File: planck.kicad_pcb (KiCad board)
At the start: 2 copper layers, 113 x 75 mm, 54 parts, among them J1 C128990, J2 USB_C_U262-161N-4BVC11, J3 C128990, SW1 SW_Cherry_MX_1.00u, SW10 SW_Cherry_MX_1.00u, SW11 SW_Cherry_MX_1.00u, SW12 SW_Cherry_MX_1.00u, SW13 SW_Cherry_MX_1.00u, SW14 SW_Cherry_MX_1.00u, SW15 SW_Cherry_MX_1.00u, SW16 SW_Cherry_MX_1.00u, SW17 SW_Cherry_MX_1.00u, SW18 SW_Cherry_MX_1.00u, SW19 SW_Cherry_MX_1.00u, SW2 SW_Cherry_MX_1.00u, SW20 SW_Cherry_MX_1.00u, SW21 SW_Cherry_MX_1.00u, SW22 SW_Cherry_MX_1.00u, SW23 SW_Cherry_MX_1.00u, SW24 SW_Cherry_MX_1.00u, SW3 SW_Cherry_MX_1.00u, SW4 SW_Cherry_MX_1.00u, SW5 SW_Cherry_MX_1.00u, SW6 SW_Cherry_MX_1.00u, SW7 SW_Cherry_MX_1.00u, SW8 SW_Cherry_MX_1.00u, SW9 SW_Cherry_MX_1.00u, U2 RP2040

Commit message: some modifications
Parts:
- removed J3: C128990, C128990:C128990_3.5MM_TRRS
- removed U2: RP2040, RP2040_minimal:RP2040-QFN-56
- added U1: RP2040, RP2040_minimal:RP2040-QFN-56, B.Cu at (139.0, 97.5)
- added Y1: 32M, Crystal:Crystal_SMD_3225-4Pin_3.2x2.5mm, B.Cu at (133.9, 121.2)
- J1: value C128990 -> USB_C_U262-161N-4BVC11; footprint C128990:C128990_3.5MM_TRRS -> josh-connectors:USB_C_U262-161N-4BVC11
- moved J2 37.8 mm to (101.2, 65.2)
- moved J1 4.66 mm to (177.0, 64.6)
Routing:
- net r1: track 239.1 -> 118.0 mm, vias 4 -> 3
- net Net-(J2-PadA5): track 2.96 -> 0.00 mm
- net Net-(J2-PadB5): track 2.53 -> 0.00 mm
- net r3: track 104.2 -> 103.2 mm

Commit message: MX version complete
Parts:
- added C1: 2.2uF ±10% 10V, Resistor_SMD:R_0201_0603Metric, B.Cu at (99.1, 69.7)
- added C10: 100nF ±10% 25V 0201, Resistor_SMD:R_0201_0603Metric, B.Cu at (138.2, 92.5)
- added C11: 100nF ±10% 25V 0201, Resistor_SMD:R_0201_0603Metric, B.Cu at (144.0, 98.5)
- added C12: 100nF ±10% 25V 0201, Resistor_SMD:R_0201_0603Metric, B.Cu at (138.3, 102.5)
- added C13: 100nF ±10% 25V 0201, Resistor_SMD:R_0201_0603Metric, B.Cu at (138.9, 92.5)
- added C14: 1uF ±20% 6.3V 0201, Capacitor_SMD:C_0201_0603Metric, B.Cu at (137.0, 92.5)
- added C15: 100nF ±10% 25V 0201, Resistor_SMD:R_0201_0603Metric, B.Cu at (136.2, 92.5)
- added C16: 100nF ±10% 25V 0201, Resistor_SMD:R_0201_0603Metric, B.Cu at (137.2, 102.5)
- added C2: 2.2uF ±10% 10V, Resistor_SMD:R_0201_0603Metric, B.Cu at (99.0, 74.7)
- added C3: 22pF ±5% 50V 0603, Resistor_SMD:R_0201_0603Metric, B.Cu at (141.5, 104.4)
- added C4: 22pF ±5% 50V 0603, Resistor_SMD:R_0201_0603Metric, B.Cu at (136.5, 104.9)
- added C5: 100nF ±10% 25V 0201, Resistor_SMD:R_0201_0603Metric, B.Cu at (144.0, 92.6)
- added C6: 1uF ±20% 6.3V 0201, Capacitor_SMD:C_0201_0603Metric, B.Cu at (134.1, 94.2)
- added C7: 100nF ±10% 25V 0201, Resistor_SMD:R_0201_0603Metric, B.Cu at (134.1, 94.9)
- added C8: 100nF ±10% 25V 0201, Resistor_SMD:R_0201_0603Metric, B.Cu at (144.0, 94.2)
- added C9: 100nF ±10% 25V 0201, Resistor_SMD:R_0201_0603Metric, B.Cu at (134.1, 98.4)
- added H1: MountingHole, MountingHole:MountingHole_2.7mm_M2.5, F.Cu at (101.0, 78.5)
- added H2: MountingHole, MountingHole:MountingHole_2.7mm_M2.5, F.Cu at (177.0, 78.5)
- added H3: MountingHole, MountingHole:MountingHole_2.7mm_M2.5, F.Cu at (177.0, 116.5)
- added H4: MountingHole, MountingHole:MountingHole_2.7mm_M2.5, F.Cu at (101.0, 116.4)
- added R3: 1kΩ ±1% 50mW 0201, Resistor_SMD:R_0201_0603Metric, B.Cu at (137.6, 103.9)
- added R4: 100Ω ±1% 50mW, Resistor_SMD:R_0201_0603Metric, B.Cu at (144.0, 95.0)
- added R5: 27Ω ±1% 50mW 0201, Resistor_SMD:R_0201_0603Metric, B.Cu at (137.9, 91.1)
- added R6: 27Ω ±1% 50mW 0201, Resistor_SMD:R_0201_0603Metric, B.Cu at (137.2, 91.1)
- added R7: 100Ω ±1% 50mW, Resistor_SMD:R_0201_0603Metric, B.Cu at (144.0, 95.7)
- added R8: 10kΩ ±1% 50mW 0201, Resistor_SMD:R_0201_0603Metric, B.Cu at (144.0, 93.4)
- added R9: 1kΩ ±1% 50mW 0201, Resistor_SMD:R_0201_0603Metric, B.Cu at (142.1, 92.6)
- added SW25: SW_Push, Switches:TSC005A1618A03, B.Cu at (139.0, 75.0)
- added U2: ME6219C33M5G, Package_TO_SOT_SMD:SOT-23-5, B.Cu at (99.7, 72.2)
- added U3: W25Q16JVUXIQ, Package_SON:SON-8-1EP_3x2mm_P0.5mm_EP1.4x1.6mm, B.Cu at (143.1, 90.9)
- D1, D10, D11, D12, D13, D14, D15, D16, D17, D18, D19, D2, D20, D21, D22, D23, D24, D3, D4, D5, D6, D7, D8, D9: value 1N4148W -> 1N4148W,100V 150mA 4ns T4
- J1, J2: footprint josh-connectors:USB_C_U262-161N-4BVC11 -> josh-connectors:USB_C_TYPE-C-31-M-14
- U1: value RP2040 -> RP2040 ARM Cortex-M0 133MHz; footprint RP2040_minimal:RP2040-QFN-56 -> Package_DFN_QFN:QFN-56-1EP_7x7mm_P0.4mm_EP3.2x3.2mm_ThermalVias
- Y1: value 32M -> 32MHz ±10ppm 20pF SMD3225-4P
- moved R2 38.9 mm to (102.6, 69.0), turned to 180 degrees
- moved R1 37.4 mm to (99.1, 69.0), turned to 0 degrees
- moved Y1 16.5 mm to (139.0, 105.5), turned to -135 degrees
- moved J2 0.85 mm to (101.2, 64.3)
- moved J1 0.22 mm to (177.0, 64.4), turned to 0 degrees
- turned U1 to 180 degrees
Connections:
- net /d+ renamed /D-
- net /d- renamed /D+
- U1 pad 1: unconnected-(U1-Pad1) -> /V3V3
- U1 pad 10: unconnected-(U1-Pad10) -> /V3V3
- U1 pad 14: unconnected-(U1-Pad14) -> c6
- U1 pad 15: unconnected-(U1-Pad15) -> c5
- U1 pad 16: unconnected-(U1-Pad16) -> c4
- U1 pad 19: unconnected-(U1-Pad19) -> GND
- U1 pad 2: unconnected-(U1-Pad2) -> /tx0
- U1 pad 20: unconnected-(U1-Pad20) -> /X32MI
- U1 pad 21: unconnected-(U1-Pad21) -> /X32MO
- U1 pad 22: unconnected-(U1-Pad22) -> /V3V3
- U1 pad 23: unconnected-(U1-Pad23) -> /V1V1
- U1 pad 28: unconnected-(U1-Pad28) -> r4
- U1 pad 29: unconnected-(U1-Pad29) -> r3
- U1 pad 3: unconnected-(U1-Pad3) -> /rx0
- U1 pad 30: unconnected-(U1-Pad30) -> c3
- U1 pad 31: unconnected-(U1-Pad31) -> c2
- U1 pad 32: unconnected-(U1-Pad32) -> c1
- U1 pad 33: unconnected-(U1-Pad33) -> /V3V3
- U1 pad 4: unconnected-(U1-Pad4) -> r1
- U1 pad 42: unconnected-(U1-Pad42) -> /V3V3
- U1 pad 43: unconnected-(U1-Pad43) -> /V3V3
- U1 pad 44: unconnected-(U1-Pad44) -> /V3V3
- U1 pad 45: unconnected-(U1-Pad45) -> /V1V1
- U1 pad 46: unconnected-(U1-Pad46) -> Net-(R6-Pad1)
- U1 pad 47: unconnected-(U1-Pad47) -> Net-(R5-Pad1)
- U1 pad 48: unconnected-(U1-Pad48) -> /V3V3
- U1 pad 49: unconnected-(U1-Pad49) -> /V3V3
- U1 pad 5: unconnected-(U1-Pad5) -> r2
- U1 pad 50: unconnected-(U1-Pad50) -> /V1V1
- U1 pad 51: unconnected-(U1-Pad51) -> /QSPI_SD3
- U1 pad 52: unconnected-(U1-Pad52) -> /QSPI_CLK
- U1 pad 53: unconnected-(U1-Pad53) -> /QSPI_SD0
- U1 pad 54: unconnected-(U1-Pad54) -> /QSPI_SD2
- U1 pad 55: unconnected-(U1-Pad55) -> /QSPI_SD1
- U1 pad 56: unconnected-(U1-Pad56) -> /QSPI_SS
- U1 pad 57: unconnected-(U1-Pad57) -> GND
- Y1 pad 3: /X32MO -> Net-(C4-Pad1)
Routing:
- net /VBUS: track 0.00 -> 123.6 mm, vias 0 -> 4
- net /V3V3: track 0.00 -> 76.6 mm, vias 0 -> 2
- net Net-(J1-PadA6): track 0.00 -> 65.6 mm, vias 0 -> 2
- net Net-(J1-PadA7): track 0.00 -> 64.9 mm, vias 0 -> 2
- net /D-: track 0.00 -> 59.5 mm, vias 0 -> 2
- net /D+: track 0.00 -> 58.6 mm
- net r2: track 182.5 -> 124.3 mm
- net c6: track 62.4 -> 118.3 mm, vias 4 -> 7
- net r1: track 118.0 -> 165.4 mm, vias 3 -> 4
- net c5: track 62.4 -> 102.8 mm, vias 4 -> 7
- net c1: track 62.5 -> 101.4 mm, vias 4 -> 5
- net c4: track 62.4 -> 91.1 mm, vias 4 -> 7
- net Net-(R9-Pad1): track 0.00 -> 23.9 mm, vias 0 -> 2
- net r4: track 104.2 -> 127.3 mm, vias 0 -> 2
- net r3: track 103.2 -> 119.4 mm, vias 0 -> 2
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- added copper zone on B.Cu, net /V3V3
- added copper zone on F.Cu, net GND
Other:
- outline, holes or cut-outs redrawn
- board text added: "boot"

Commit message: add libraries
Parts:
- U1: footprint Package_DFN_QFN:QFN-56-1EP_7x7mm_P0.4mm_EP3.2x3.2mm_ThermalVias -> MCU_RaspberryPi_and_Boards:RP2040-QFN-56

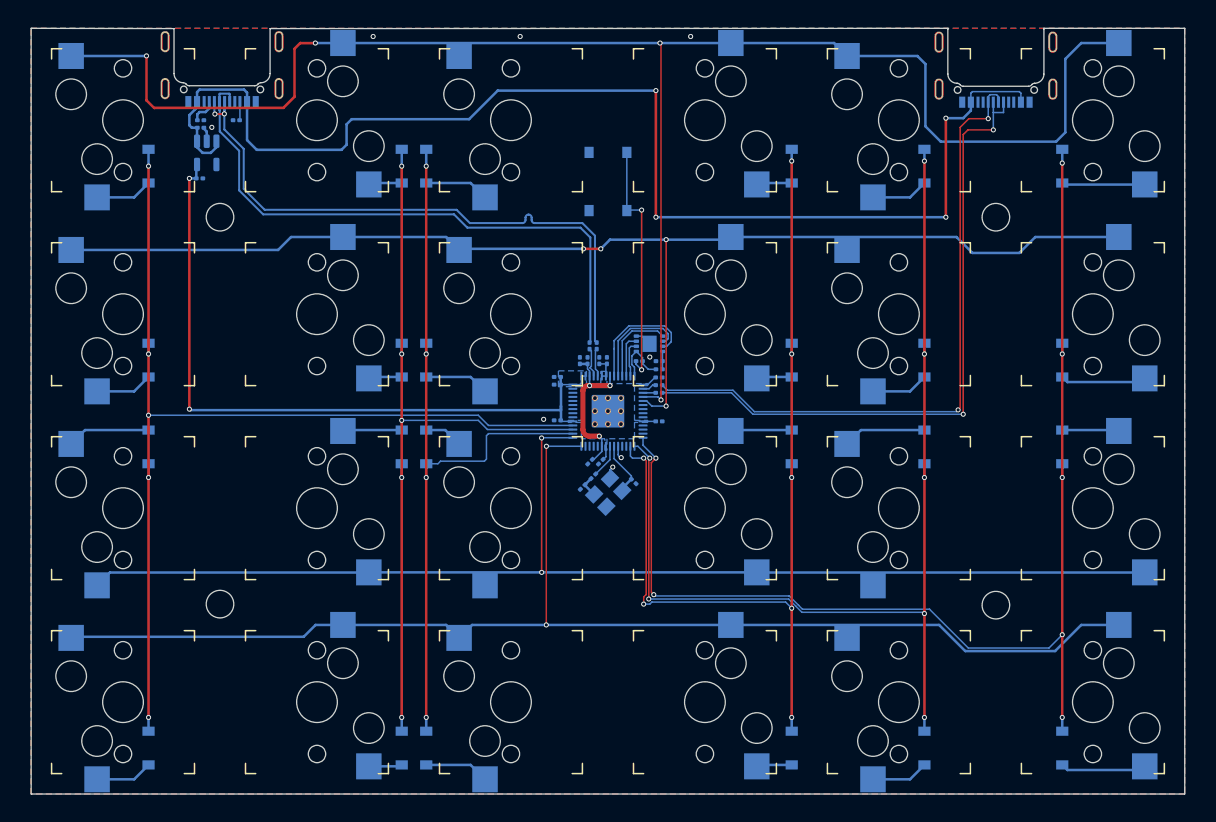
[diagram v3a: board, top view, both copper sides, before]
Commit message: add choc libraries
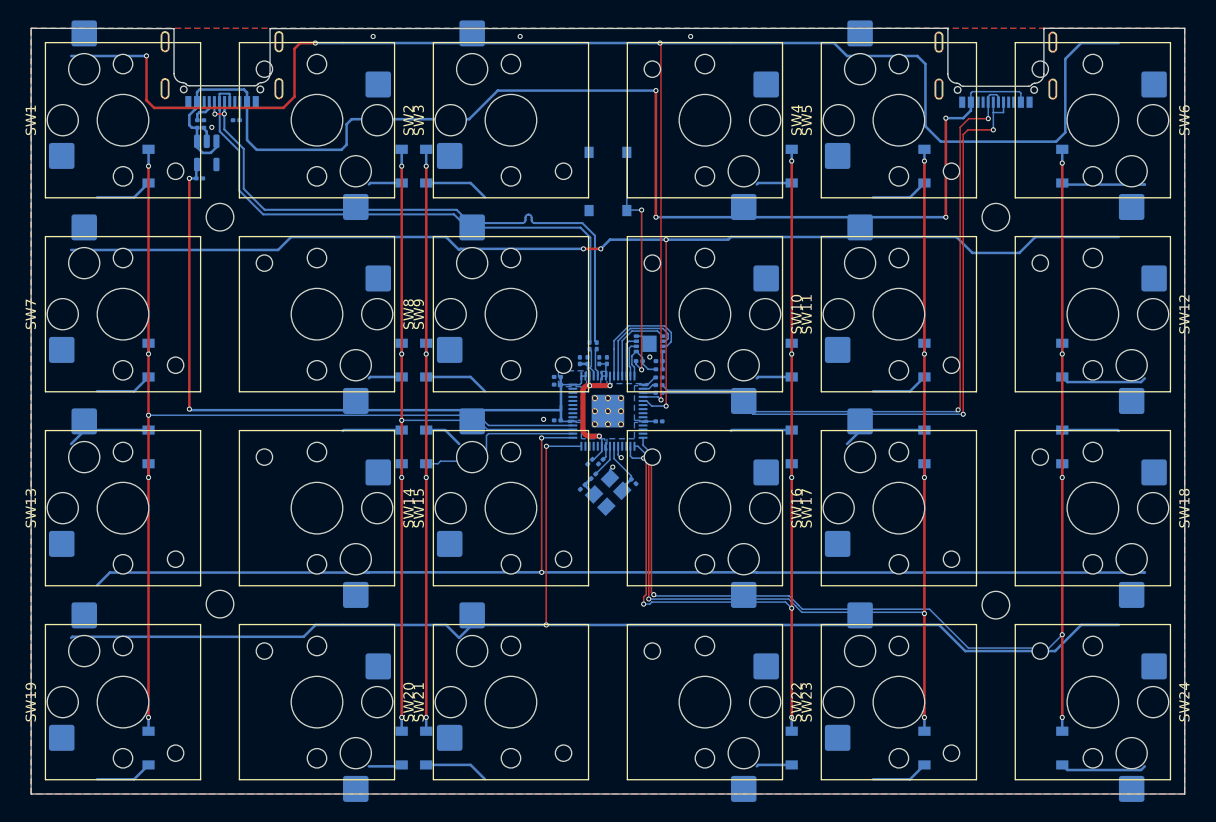
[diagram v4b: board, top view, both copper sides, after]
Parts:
- SW1, SW10, SW11, SW12, SW13, SW14, SW15, SW16, SW17, SW18, SW19, SW2, SW20, SW21, SW22, SW23, SW24, SW3, SW4, SW5, SW6, SW7, SW8, SW9: footprint Switches:SW_Cherry_MX_1.00u_Plate_HS -> Switch_Keyboard_Hotswap_Kailh:SW_Hotswap_Kailh_Choc_V1V2
- turned SW1 to 90 degrees
- turned SW10 to -90 degrees
- turned SW11 to 90 degrees
- turned SW12 to -90 degrees
- turned SW13 to 90 degrees
- turned SW14 to -90 degrees
- turned SW15 to 90 degrees
- turned SW16 to -90 degrees
- turned SW17 to 90 degrees
- turned SW18 to -90 degrees
- turned SW19 to 90 degrees
- turned SW2 to -90 degrees
- turned SW20 to -90 degrees
- turned SW21 to 90 degrees
- turned SW22 to -90 degrees
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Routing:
- net /VBUS: track 123.6 -> 684.4 mm, vias 4 -> 31
- net c6: track 118.3 -> 0.00 mm, vias 7 -> 0
- net c5: track 102.8 -> 0.00 mm, vias 7 -> 0
- net c4: track 91.1 -> 0.00 mm, vias 7 -> 0
- net Net-(J1-PadA6): track 65.6 -> 0.00 mm, vias 2 -> 0
- net Net-(J1-PadA7): track 64.9 -> 0.00 mm, vias 2 -> 0
- net /D-: track 59.5 -> 0.00 mm, vias 2 -> 0
- net /D+: track 58.6 -> 0.00 mm
- net GND: vias 8 -> 7
- net /QSPI_SS: vias 0 -> 1

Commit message: main layouts
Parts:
- removed J1: USB_C_U262-161N-4BVC11, josh-connectors:USB_C_TYPE-C-31-M-14
- removed R4, R7: 100Ω ±1% 50mW, Resistor_SMD:R_0201_0603Metric
- added C17: 100nF ±10% 25V 0201, Resistor_SMD:R_0201_0603Metric, B.Cu at (143.8, 131.4)
- added C18: 100nF ±10% 25V 0201, Resistor_SMD:R_0201_0603Metric, B.Cu at (152.3, 101.5)
- added C19: 100nF ±10% 25V 0201, Resistor_SMD:R_0201_0603Metric, B.Cu at (191.2, 101.4)
- added C20: 100nF ±10% 25V 0201, Resistor_SMD:R_0201_0603Metric, B.Cu at (115.2, 63.5)
- added C21: 100nF ±10% 25V 0201, Resistor_SMD:R_0201_0603Metric, B.Cu at (96.2, 63.4)
- added C22: 100nF ±10% 25V 0201, Resistor_SMD:R_0201_0603Metric, B.Cu at (162.8, 93.5)
- added C23: 100nF ±10% 25V 0201, Resistor_SMD:R_0201_0603Metric, B.Cu at (86.8, 93.6)
- added C24: 100nF ±10% 25V 0201, Resistor_SMD:R_0201_0603Metric, B.Cu at (124.8, 131.6)
- added C25: 100nF ±10% 25V 0201, Resistor_SMD:R_0201_0603Metric, B.Cu at (115.2, 101.5)
- added C26: 100nF ±10% 25V 0201, Resistor_SMD:R_0201_0603Metric, B.Cu at (172.2, 101.5)
- added C27: 100nF ±10% 25V 0201, Resistor_SMD:R_0201_0603Metric, B.Cu at (181.8, 93.6)
- added C28: 100nF ±10% 25V 0201, Resistor_SMD:R_0201_0603Metric, B.Cu at (125.7, 93.5)
- added C29: 100nF ±10% 25V 0201, Resistor_SMD:R_0201_0603Metric, B.Cu at (146.3, 94.9)
- added C30: 100nF ±10% 25V 0201, Resistor_SMD:R_0201_0603Metric, B.Cu at (105.8, 93.5)
- added C31: 100nF ±10% 25V 0201, Resistor_SMD:R_0201_0603Metric, B.Cu at (105.8, 131.4)
- added C32: 100nF ±10% 25V 0201, Resistor_SMD:R_0201_0603Metric, B.Cu at (96.2, 101.5)
- added C33: 100nF ±10% 25V 0201, Resistor_SMD:R_0201_0603Metric, B.Cu at (133.4, 101.5)
- added C34: 100nF ±10% 25V 0201, Resistor_SMD:R_0201_0603Metric, B.Cu at (191.2, 63.4)
- added C35: 100nF ±10% 25V 0201, Resistor_SMD:R_0201_0603Metric, B.Cu at (172.2, 63.4)
- added C36: 100nF ±10% 25V 0201, Resistor_SMD:R_0201_0603Metric, B.Cu at (152.3, 63.5)
- added C37: 100nF ±10% 25V 0201, Resistor_SMD:R_0201_0603Metric, B.Cu at (131.2, 62.2)
- added C38: 100nF ±10% 25V 0201, Resistor_SMD:R_0201_0603Metric, B.Cu at (86.8, 131.4)
- added C39: 100nF ±10% 25V 0201, Resistor_SMD:R_0201_0603Metric, B.Cu at (181.8, 131.4)
- added C40: 100nF ±10% 25V 0201, Resistor_SMD:R_0201_0603Metric, B.Cu at (162.8, 131.4)
- added D25: WS2812B, MCU_RaspberryPi_and_Boards:WS2812_6028_REV, F.Cu at (91.5, 64.2)
- added D26: WS2812B, MCU_RaspberryPi_and_Boards:WS2812_6028_REV, F.Cu at (110.5, 64.3)
- added D27: WS2812B, MCU_RaspberryPi_and_Boards:WS2812_6028_REV_S, F.Cu at (129.5, 64.3)
- added D28: WS2812B, MCU_RaspberryPi_and_Boards:WS2812_6028_REV_S, F.Cu at (148.5, 64.3)
- added D29: WS2812B, MCU_RaspberryPi_and_Boards:WS2812_6028_REV, F.Cu at (167.5, 64.2)
- added D30: WS2812B, MCU_RaspberryPi_and_Boards:WS2812_6028_REV, F.Cu at (186.5, 64.2)
- added D31: WS2812B, MCU_RaspberryPi_and_Boards:WS2812_6028_REV, F.Cu at (186.5, 92.8)
- added D32: WS2812B, MCU_RaspberryPi_and_Boards:WS2812_6028_REV, F.Cu at (167.5, 92.7)
- added D33: WS2812B, MCU_RaspberryPi_and_Boards:WS2812_6028_REV_S, F.Cu at (148.5, 92.7)
- added D34: WS2812B, MCU_RaspberryPi_and_Boards:WS2812_6028_REV_S, F.Cu at (129.5, 92.7)
- added D35: WS2812B, MCU_RaspberryPi_and_Boards:WS2812_6028_REV, F.Cu at (110.5, 92.7)
- added D36: WS2812B, MCU_RaspberryPi_and_Boards:WS2812_6028_REV, F.Cu at (91.5, 92.8)
- added D37: WS2812B, MCU_RaspberryPi_and_Boards:WS2812_6028_REV, F.Cu at (91.5, 102.3)
- added D38: WS2812B, MCU_RaspberryPi_and_Boards:WS2812_6028_REV, F.Cu at (110.5, 102.3)
- added D39: WS2812B, MCU_RaspberryPi_and_Boards:WS2812_6028_REV_S, F.Cu at (129.5, 102.3)
- added D40: WS2812B, MCU_RaspberryPi_and_Boards:WS2812_6028_REV_S, F.Cu at (148.5, 102.3)
- added D41: WS2812B, MCU_RaspberryPi_and_Boards:WS2812_6028_REV, F.Cu at (167.5, 102.3)
- added D42: WS2812B, MCU_RaspberryPi_and_Boards:WS2812_6028_REV, F.Cu at (186.5, 102.2)
- added D43: WS2812B, MCU_RaspberryPi_and_Boards:WS2812_6028_REV, F.Cu at (186.5, 130.7)
- added D44: WS2812B, MCU_RaspberryPi_and_Boards:WS2812_6028_REV, F.Cu at (167.5, 130.7)
- added D45: WS2812B, MCU_RaspberryPi_and_Boards:WS2812_6028_REV, F.Cu at (148.5, 130.7)
- added D46: WS2812B, MCU_RaspberryPi_and_Boards:WS2812_6028_REV, F.Cu at (129.5, 130.8)
- added D47: WS2812B, MCU_RaspberryPi_and_Boards:WS2812_6028_REV, F.Cu at (110.5, 130.7)
- added D48: WS2812B, MCU_RaspberryPi_and_Boards:WS2812_6028_REV, F.Cu at (91.5, 130.7)
- SW1, SW10, SW11, SW12, SW13, SW14, SW15, SW16, SW17, SW18, SW19, SW2, SW20, SW21, SW22, SW23, SW24, SW3, SW4, SW5, SW6, SW7, SW8, SW9: value SW_Cherry_MX_1.00u -> SW_Hotswap_Kailh_Choc_V1_1u; footprint Switch_Keyboard_Hotswap_Kailh:SW_Hotswap_Kailh_Choc_V1V2 -> Switch_Keyboard_Kailh:SW_Hotswap_Kailh_Choc_V1
- moved C1 46.9 mm to (145.3, 77.8), turned to -90 degrees
- moved U2 43.6 mm to (142.8, 78.5), turned to 180 degrees
- moved C2 41.4 mm to (140.3, 77.8), turned to -90 degrees
- moved R1 38.7 mm to (137.8, 68.9), turned to -90 degrees
- moved R2 38.2 mm to (140.8, 68.9), turned to -90 degrees
- moved J2 37.8 mm to (139.0, 64.3)
- moved SW25 29.4 mm to (158.0, 97.5), turned to 0 degrees
- moved D15 19.8 mm to (134.9, 115.3), turned to 0 degrees
- moved D9 18.8 mm to (134.9, 79.7), turned to 0 degrees
- moved D21 18.8 mm to (134.9, 117.7), turned to 0 degrees
- moved D18 16.6 mm to (191.9, 115.3), turned to 0 degrees
- moved D13 16.4 mm to (86.1, 115.3), turned to 180 degrees
- moved D17 16.4 mm to (162.1, 115.3), turned to 180 degrees
- moved D12 15.4 mm to (191.9, 79.7), turned to 0 degrees
- moved D24 15.4 mm to (191.9, 117.7), turned to 0 degrees
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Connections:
- D10 pad 1: Net-(D10-Pad1) -> Net-(D10-K)
- D12 pad 1: Net-(D12-Pad1) -> Net-(D12-K)
- D13 pad 1: Net-(D13-Pad1) -> Net-(D13-K)
- D15 pad 1: Net-(D15-Pad1) -> Net-(D15-K)
- D17 pad 1: Net-(D17-Pad1) -> Net-(D17-K)
- D19 pad 1: Net-(D19-Pad1) -> Net-(D19-K)
- D2 pad 1: Net-(D2-Pad1) -> Net-(D2-K)
- D21 pad 1: Net-(D21-Pad1) -> Net-(D21-K)
- D23 pad 1: Net-(D23-Pad1) -> Net-(D23-K)
- D4 pad 1: Net-(D4-Pad1) -> Net-(D4-K)
- D6 pad 1: Net-(D6-Pad1) -> Net-(D6-K)
- D8 pad 1: Net-(D8-Pad1) -> Net-(D8-K)
- SW10 pad 1: r2 -> Net-(D10-K)
- SW10 pad 2: Net-(D10-Pad1) -> r2
- SW12 pad 1: r2 -> Net-(D12-K)
- SW12 pad 2: Net-(D12-Pad1) -> r2
- SW13 pad 1: r3 -> Net-(D13-K)
- SW13 pad 2: Net-(D13-Pad1) -> r3
- SW15 pad 1: r3 -> Net-(D15-K)
- SW15 pad 2: Net-(D15-Pad1) -> r3
- SW17 pad 1: r3 -> Net-(D17-K)
- SW17 pad 2: Net-(D17-Pad1) -> r3
- SW19 pad 1: Net-(D19-Pad1) -> r4
- SW19 pad 2: r4 -> Net-(D19-K)
- SW2 pad 1: r1 -> Net-(D2-K)
- SW2 pad 2: Net-(D2-Pad1) -> r1
- SW21 pad 1: Net-(D21-Pad1) -> r4
- SW21 pad 2: r4 -> Net-(D21-K)
- SW23 pad 1: Net-(D23-Pad1) -> r4
- SW23 pad 2: r4 -> Net-(D23-K)
- SW4 pad 1: r1 -> Net-(D4-K)
- SW4 pad 2: Net-(D4-Pad1) -> r1
- SW6 pad 1: r1 -> Net-(D6-K)
- SW6 pad 2: Net-(D6-Pad1) -> r1
- SW8 pad 1: r2 -> Net-(D8-K)
- SW8 pad 2: Net-(D8-Pad1) -> r2
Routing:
- net /VBUS: track 684.4 -> 356.5 mm, vias 31 -> 0
- net c3: track 76.3 -> 4.60 mm, vias 4 -> 0
- net /V3V3: track 76.6 -> 10.2 mm, vias 2 -> 0
- net c1: track 101.4 -> 42.2 mm, vias 5 -> 2
- net r1: track 165.4 -> 108.0 mm, vias 4 -> 2
- net c5: track 0.00 -> 42.3 mm, vias 0 -> 2
- net Net-(D30-DOUT): track 0.00 -> 40.5 mm, vias 0 -> 2
- net Net-(D42-DOUT): track 0.00 -> 40.3 mm, vias 0 -> 2
- net c6: track 0.00 -> 40.3 mm, vias 0 -> 2
- net c4: track 0.00 -> 40.3 mm, vias 0 -> 2
- net c2: track 76.5 -> 40.3 mm, vias 5 -> 2
- net /D+: track 0.00 -> 29.6 mm, vias 0 -> 2
- net /D-: track 0.00 -> 28.7 mm
- net Net-(R9-Pad1): track 23.9 -> 0.00 mm, vias 2 -> 0
- net r2: track 124.3 -> 103.5 mm, vias 4 -> 2
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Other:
- board size 113 x 75 mm -> 115 x 75 mm
- board text added: "BOOT"
- board text removed: "boot"

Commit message: ...
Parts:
- moved C8 1.57 mm to (140.8, 89.0), turned to 180 degrees
- moved C2 0.65 mm to (140.3, 77.2), turned to 90 degrees
- moved R2 0.53 mm to (140.3, 69.2)
- moved R1 0.35 mm to (137.8, 69.2)
- moved C1 0.06 mm to (145.3, 77.9)
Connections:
- C5 pad 2: Net-(U3-VCC) -> /V3V3
- R8 pad 2: Net-(U3-VCC) -> /V3V3
- U3 pad 8: Net-(U3-VCC) -> /V3V3
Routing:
- net /VBUS: track 356.5 -> 629.7 mm, vias 0 -> 10
- net c1: track 42.2 -> 94.8 mm, vias 2 -> 3
- net Net-(D39-DOUT): track 0.00 -> 25.6 mm
- net r4: track 112.6 -> 138.1 mm, vias 0 -> 2
- net /V3V3: track 10.2 -> 29.8 mm, vias 0 -> 2
- net c2: track 40.3 -> 58.3 mm, vias 2 -> 3
- net r3: track 103.7 -> 117.3 mm, vias 0 -> 2
- net /V1V1: track 3.16 -> 14.6 mm, vias 0 -> 3
- net Net-(U3-VCC): track 1.56 -> 0.00 mm
- net Net-(D18-K): track 3.30 -> 2.45 mm
- net Net-(D36-DOUT): track 15.1 -> 15.8 mm, vias 0 -> 2
- net Net-(J2-CC2): track 1.39 -> 1.91 mm

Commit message: layout
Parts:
- added J1: USB_C_U262-161N-4BVC11, josh-connectors:USB_C_TYPE-C-31-M-14, B.Cu at (176.9, 64.3)
- added J3: USB_C_U262-161N-4BVC11, josh-connectors:USB_C_TYPE-C-31-M-14, B.Cu at (101.1, 64.3)
- moved SW25 8.50 mm to (149.5, 97.5)
- moved R9 3.92 mm to (143.9, 94.2)
- moved C29 2.25 mm to (145.0, 93.1), turned to -90 degrees
- moved C37 0.50 mm to (131.7, 62.0), turned to -90 degrees
- moved C3 0.15 mm to (139.7, 102.4)
- moved R3 0.15 mm to (139.7, 104.4)
- moved C22 0.07 mm to (162.8, 93.5)
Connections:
- SW13 pad 1: Net-(D13-K) -> r3
- SW13 pad 2: r3 -> Net-(D13-K)
- SW19 pad 1: r4 -> Net-(D19-K)
- SW19 pad 2: Net-(D19-K) -> r4
- SW20 pad 1: r4 -> Net-(D20-K)
- SW20 pad 2: Net-(D20-K) -> r4
- SW21 pad 1: r4 -> Net-(D21-K)
- SW21 pad 2: Net-(D21-K) -> r4
- SW22 pad 1: r4 -> Net-(D22-K)
- SW22 pad 2: Net-(D22-K) -> r4
- SW23 pad 1: r4 -> Net-(D23-K)
- SW23 pad 2: Net-(D23-K) -> r4
- U1 pad 14: c6 -> unconnected-(U1-GPIO11-Pad14)
- U1 pad 16: c4 -> unconnected-(U1-GPIO13-Pad16)
- U1 pad 29: r3 -> c3
- U1 pad 30: c3 -> unconnected-(U1-GPIO19-Pad30)
- U1 pad 34: unconnected-(U1-GPIO22-Pad34) -> r3
- U1 pad 37: unconnected-(U1-GPIO25-Pad37) -> r1
- U1 pad 4: r1 -> unconnected-(U1-GPIO2-Pad4)
- U1 pad 5: r2 -> unconnected-(U1-GPIO3-Pad5)
- U1 pad 7: unconnected-(U1-GPIO5-Pad7) -> r2
- U1 pad 8: unconnected-(U1-GPIO6-Pad8) -> c6
- U1 pad 9: unconnected-(U1-GPIO7-Pad9) -> c4
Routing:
- net c3: track 4.60 -> 92.1 mm, vias 0 -> 4
- net c6: track 40.3 -> 96.6 mm, vias 2 -> 3
- net r1: track 108.0 -> 154.8 mm, vias 2 -> 8
- net /VBUS: track 629.7 -> 584.4 mm, vias 10 -> 17
- net Net-(D27-DOUT): track 0.00 -> 27.5 mm, vias 0 -> 6
- net Net-(D33-DOUT): track 0.00 -> 26.2 mm, vias 0 -> 6
- net r4: track 138.1 -> 114.8 mm
- net r2: track 103.5 -> 126.7 mm, vias 2 -> 4
- net c5: track 42.3 -> 60.0 mm, vias 2 -> 3
- net c4: track 40.3 -> 56.0 mm, vias 2 -> 3
- net /tx0: track 0.00 -> 14.0 mm
- net /rx0: track 0.00 -> 13.8 mm
- net Net-(D23-K): track 14.1 -> 2.45 mm
- net Net-(D19-K): track 14.1 -> 2.45 mm
- net Net-(R9-Pad1): track 0.00 -> 8.73 mm
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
